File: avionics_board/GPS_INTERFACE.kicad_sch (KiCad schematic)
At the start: 1 part, among them J6 Conn_02x04

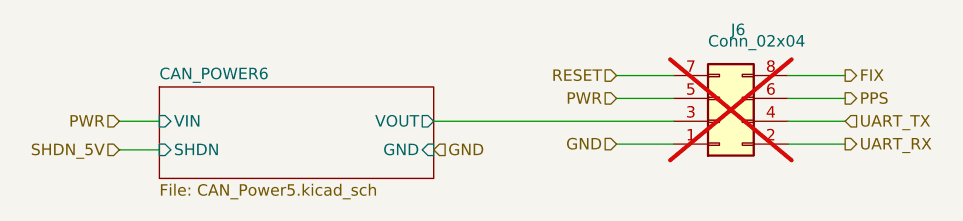
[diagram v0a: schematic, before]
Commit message: use SAMTEC connectors for AVI to side panels, try HARWIN ones next
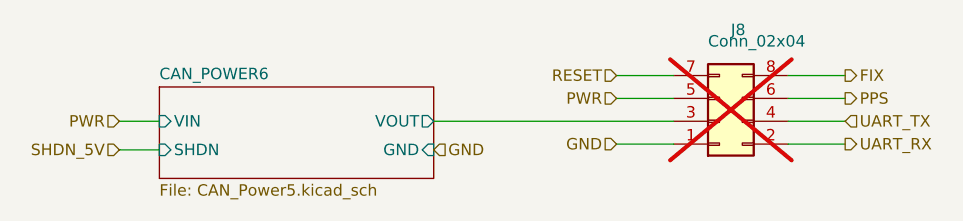
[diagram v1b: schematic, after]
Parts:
- renumbered J6 to J8
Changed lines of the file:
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@@
 		(on_board yes)
 		(dnp yes)
-		(property "Reference" "J6"
+		(property "Reference" "J8"
 			(at 171.45 95.25 0)
 			(effects
@@
 			(project "AVIONICS_BOARD"
 				(path "/f6cc00ab-17f1-4973-862f-7ac95fe70668/5de22591-2293-4710-b038-9e93720cba0f"
-					(reference "J6")
+					(reference "J8")
 					(unit 1)
 				)

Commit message: AVI: using through hole M50 connectors for sun detectors and ACS
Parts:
- J8: Order https://www.digikey.com/product-detail/en/adam-tech/PH1-05-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 -> (none)
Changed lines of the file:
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@@
-			)
-		)
-		(property "Order" "https://www.digikey.com/product-detail/en/adam-tech/PH1-05-UA/2057-PH1-05-UA-ND/9830343"
-			(at 170.18 105.41 0)
-			(effects
-				(font
-					(size 1.27 1.27)
-				)
-				(hide yes)
 			)
 		)
